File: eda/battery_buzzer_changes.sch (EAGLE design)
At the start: 15 parts, among them Q2 IRFML8244

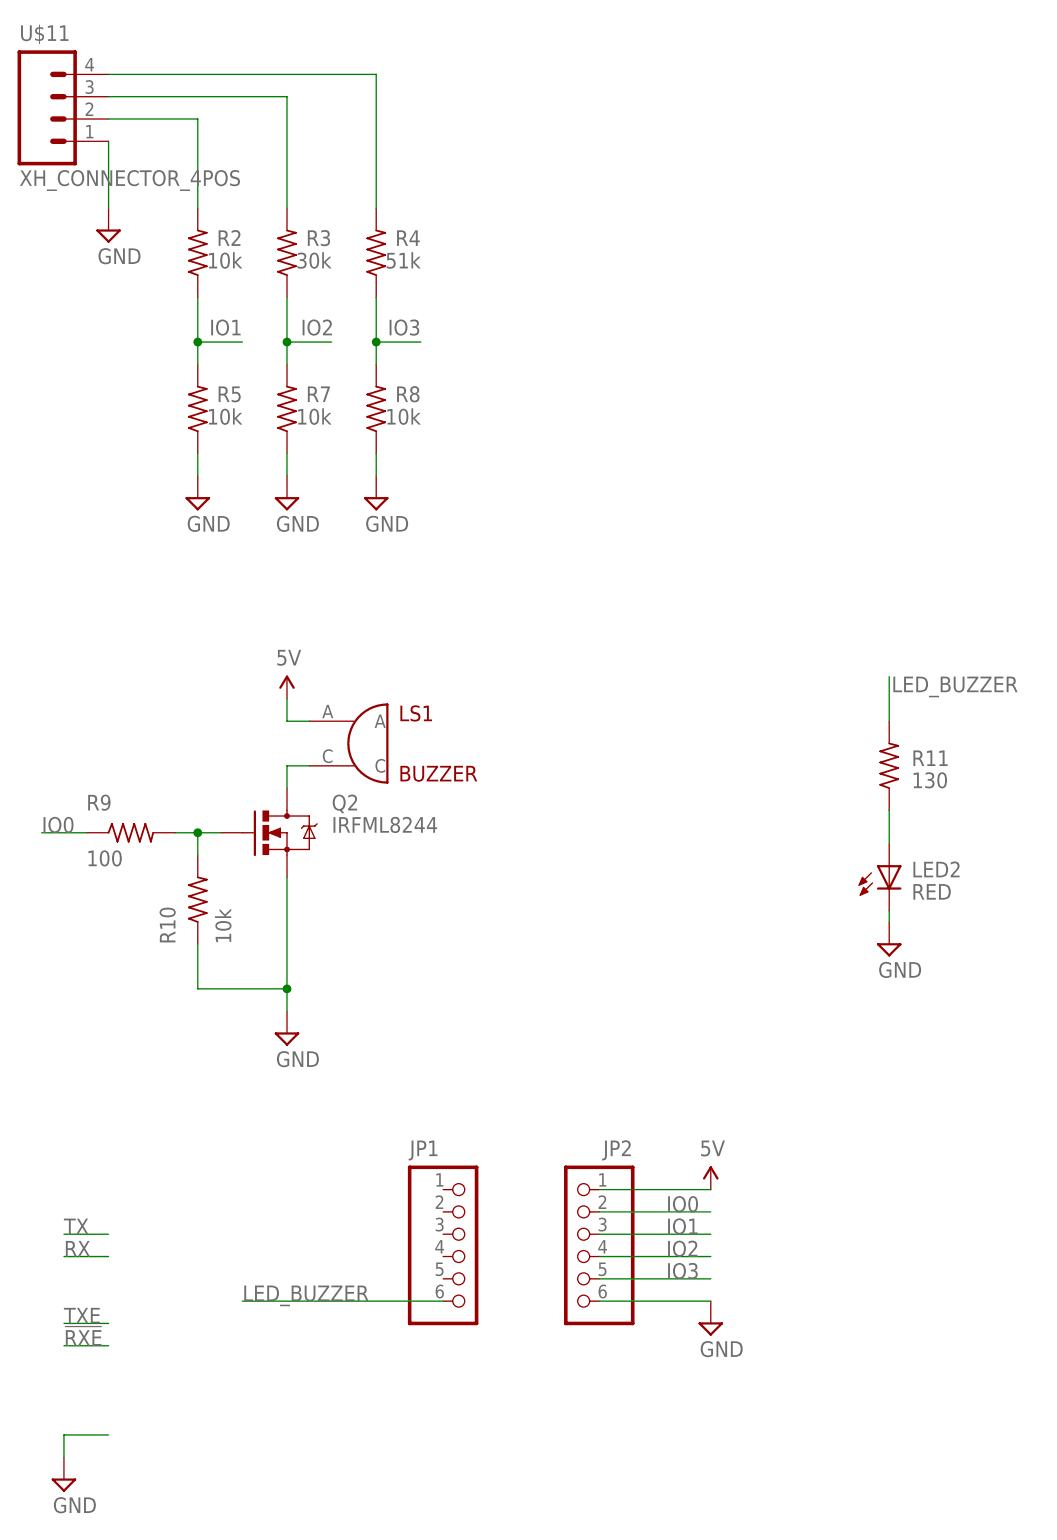
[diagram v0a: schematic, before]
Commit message: Battery Buzzer Changes
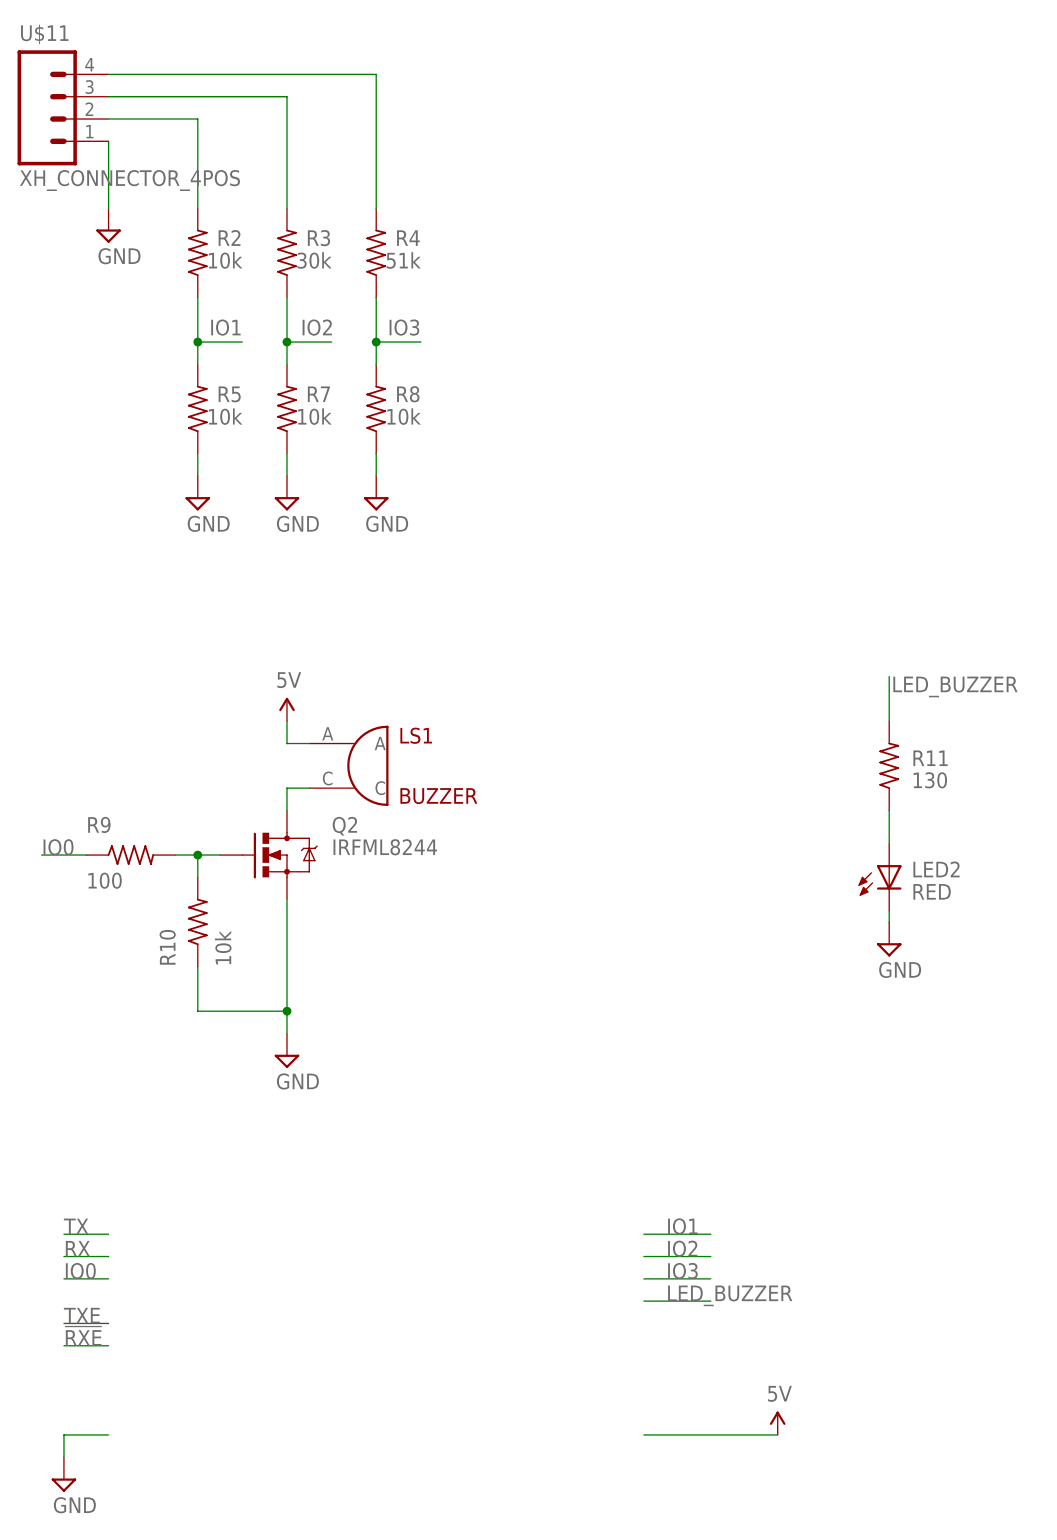
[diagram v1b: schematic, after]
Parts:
- removed JP1, JP2: (no value), pie:PINHD-1X6
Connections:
- net 5V: no longer JP2.1
- net IO0: no longer JP2.2
- net IO1: no longer JP2.3
- net IO2: no longer JP2.4
- net IO3: no longer JP2.5
- net LED_BUZZER: no longer JP1.6
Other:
- moved on the sheet: LS1, Q2, R10, R9
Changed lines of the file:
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@@
 <setting verticaltext="up"/>
 </settings>
-<grid distance="0.1" unitdist="inch" unit="inch" style="lines" multiple="1" display="yes" altdistance="0.01" altunitdist="inch" altunit="inch"/>
+<grid distance="0.1" unitdist="inch" unit="inch" style="lines" multiple="1" display="no" altdistance="0.01" altunitdist="inch" altunit="inch"/>
 <layers>
 <layer number="1" name="Top" color="4" fill="1" visible="no" active="no"/>
@@
 <part name="SUPPLY9" library="pie" deviceset="GND" device=""/>
 <part name="SUPPLY10" library="pie" deviceset="GND" device=""/>
+<part name="R11" library="pie" deviceset="R-US_" device="R0603" value="130"/>
+<part name="LED2" library="pie" deviceset="LED" device="0805" value="RED"/>
+<part name="SUPPLY13" library="pie" deviceset="GND" device=""/>
 <part name="LS1" library="pie" deviceset="BUZZER" device="" value="BUZZER"/>
 <part name="R9" library="pie" deviceset="R-US_" device="R0603" value="100"/>
@@
 <part name="U$12" library="pie" deviceset="5V" device=""/>
 <part name="SUPPLY11" library="pie" deviceset="GND" device=""/>
-<part name="R11" library="pie" deviceset="R-US_" device="R0603" value="130"/>
-<part name="LED2" library="pie" deviceset="LED" device="0805" value="RED"/>
-<part name="SUPPLY13" library="pie" deviceset="GND" device=""/>
 <part name="Q2" library="pie" deviceset="MOSFET-NCHANNEL" device="SMD" value="IRFML8244"/>
-<part name="JP1" library="pie" deviceset="PINHD-1X6" device=""/>
-<part name="JP2" library="pie" deviceset="PINHD-1X6" device=""/>
-<part name="SUPPLY2" library="pie" deviceset="GND" device=""/>
 </parts>
 <sheets>
@@
 </instance>
 <instance part="FRAME1" gate="G$2" x="147.32" y="0"/>
-<instance part="U$3" gate="G$1" x="88.9" y="43.18"/>
+<instance part="U$3" gate="G$1" x="96.52" y="15.24"/>
 <instance part="SUPPLY1" gate="GND" x="15.24" y="10.16"/>
 <instance part="U$11" gate="G$1" x="12.7" y="167.64"/>
@@
 <instance part="SUPPLY9" gate="GND" x="40.64" y="121.92"/>
 <instance part="SUPPLY10" gate="GND" x="50.8" y="121.92"/>
-<instance part="LS1" gate="G$1" x="48.26" y="93.98" smashed="yes">
-<attribute name="NAME" x="53.34" y="96.52" size="1.778" layer="94"/>
-<attribute name="VALUE" x="53.34" y="91.44" size="1.778" layer="94" align="top-left"/>
-</instance>
-<instance part="R9" gate="G$1" x="22.86" y="83.82"/>
-<instance part="R10" gate="G$1" x="30.48" y="76.2" rot="R90"/>
-<instance part="U$12" gate="G$1" x="40.64" y="99.06"/>
-<instance part="SUPPLY11" gate="GND" x="40.64" y="60.96"/>
 <instance part="R11" gate="G$1" x="109.22" y="91.44" smashed="yes" rot="R90">
 <attribute name="NAME" x="111.76" y="91.4146" size="1.778" layer="95" rot="MR0" align="bottom-right"/>
@@
 </instance>
 <instance part="SUPPLY13" gate="GND" x="109.22" y="71.12"/>
-<instance part="Q2" gate="G$1" x="40.64" y="83.82"/>
-<instance part="JP1" gate="A" x="58.42" y="36.83"/>
-<instance part="JP2" gate="A" x="76.2" y="36.83" rot="MR0"/>
-<instance part="SUPPLY2" gate="GND" x="88.9" y="27.94"/>
+<instance part="LS1" gate="G$1" x="48.26" y="91.44" smashed="yes">
+<attribute name="NAME" x="53.34" y="93.98" size="1.778" layer="94"/>
+<attribute name="VALUE" x="53.34" y="88.9" size="1.778" layer="94" align="top-left"/>
+</instance>
+<instance part="R9" gate="G$1" x="22.86" y="81.28"/>
+<instance part="R10" gate="G$1" x="30.48" y="73.66" rot="R90"/>
+<instance part="U$12" gate="G$1" x="40.64" y="96.52"/>
+<instance part="SUPPLY11" gate="GND" x="40.64" y="58.42"/>
+<instance part="Q2" gate="G$1" x="40.64" y="81.28"/>
 </instances>
 <busses>
@@
 <net name="5V" class="0">
 <segment>
+<pinref part="U$3" gate="G$1" pin="5V"/>
+<wire x1="81.28" y1="15.24" x2="96.52" y2="15.24" width="0.1524" layer="91"/>
+</segment>
+<segment>
 <pinref part="LS1" gate="G$1" pin="A"/>
 <pinref part="U$12" gate="G$1" pin="5V"/>
-<wire x1="43.18" y1="96.52" x2="40.64" y2="96.52" width="0.1524" layer="91"/>
-<wire x1="40.64" y1="96.52" x2="40.64" y2="99.06" width="0.1524" layer="91"/>
-</segment>
-<segment>
-<pinref part="U$3" gate="G$1" pin="5V"/>
-<pinref part="JP2" gate="A" pin="1"/>
-<wire x1="88.9" y1="43.18" x2="76.2" y2="43.18" width="0.1524" layer="91"/>
+<wire x1="43.18" y1="93.98" x2="40.64" y2="93.98" width="0.1524" layer="91"/>
+<wire x1="40.64" y1="93.98" x2="40.64" y2="96.52" width="0.1524" layer="91"/>
 </segment>
 </net>
@@
 </segment>
 <segment>
-<wire x1="40.64" y1="63.5" x2="40.64" y2="66.04" width="0.1524" layer="91"/>
-<pinref part="SUPPLY11" gate="GND" pin="GND"/>
-<wire x1="40.64" y1="66.04" x2="40.64" y2="78.74" width="0.1524" layer="91"/>
-<wire x1="30.48" y1="66.04" x2="40.64" y2="66.04" width="0.1524" layer="91"/>
-<junction x="40.64" y="66.04"/>
-<pinref part="Q2" gate="G$1" pin="S"/>
-<pinref part="R10" gate="G$1" pin="1"/>
-<wire x1="30.48" y1="71.12" x2="30.48" y2="66.04" width="0.1524" layer="91"/>
-</segment>
-<segment>
 <pinref part="LED2" gate="G$1" pin="C"/>
 <pinref part="SUPPLY13" gate="GND" pin="GND"/>
@@
 </segment>
 <segment>
-<wire x1="88.9" y1="30.48" x2="76.2" y2="30.48" width="0.1524" layer="91"/>
-<pinref part="SUPPLY2" gate="GND" pin="GND"/>
+<wire x1="40.64" y1="60.96" x2="40.64" y2="63.5" width="0.1524" layer="91"/>
+<pinref part="SUPPLY11" gate="GND" pin="GND"/>
+<wire x1="40.64" y1="63.5" x2="40.64" y2="76.2" width="0.1524" layer="91"/>
+<wire x1="30.48" y1="63.5" x2="40.64" y2="63.5" width="0.1524" layer="91"/>
+<junction x="40.64" y="63.5"/>
+<pinref part="Q2" gate="G$1" pin="S"/>
+<pinref part="R10" gate="G$1" pin="1"/>
+<wire x1="30.48" y1="68.58" x2="30.48" y2="63.5" width="0.1524" layer="91"/>
 </segment>
 </net>
@@
 <net name="IO1" class="0">
 <segment>
-<wire x1="76.2" y1="38.1" x2="88.9" y2="38.1" width="0.1524" layer="91"/>
+<wire x1="81.28" y1="38.1" x2="88.9" y2="38.1" width="0.1524" layer="91"/>
 <label x="83.82" y="38.1" size="1.778" layer="95"/>
-<pinref part="JP2" gate="A" pin="3"/>
 </segment>
 <segment>
@@
 <net name="IO2" class="0">
 <segment>
-<wire x1="76.2" y1="35.56" x2="88.9" y2="35.56" width="0.1524" layer="91"/>
+<wire x1="81.28" y1="35.56" x2="88.9" y2="35.56" width="0.1524" layer="91"/>
 <label x="83.82" y="35.56" size="1.778" layer="95"/>
-<pinref part="JP2" gate="A" pin="4"/>
 </segment>
 <segment>
@@
 <net name="IO0" class="0">
 <segment>
+<wire x1="20.32" y1="33.02" x2="15.24" y2="33.02" width="0.1524" layer="91"/>
+<label x="15.24" y="33.02" size="1.778" layer="95"/>
+</segment>
+<segment>
 <pinref part="R9" gate="G$1" pin="1"/>
-<wire x1="17.78" y1="83.82" x2="12.7" y2="83.82" width="0.1524" layer="91"/>
-<label x="12.7" y="83.82" size="1.778" layer="95"/>
-</segment>
-<segment>
-<label x="83.82" y="40.64" size="1.778" layer="95"/>
-<pinref part="JP2" gate="A" pin="2"/>
-<wire x1="76.2" y1="40.64" x2="88.9" y2="40.64" width="0.1524" layer="91"/>
+<wire x1="17.78" y1="81.28" x2="12.7" y2="81.28" width="0.1524" layer="91"/>
+<label x="12.7" y="81.28" size="1.778" layer="95"/>
 </segment>
 </net>
 <net name="IO3" class="0">
 <segment>
-<wire x1="76.2" y1="33.02" x2="88.9" y2="33.02" width="0.1524" layer="91"/>
+<wire x1="81.28" y1="33.02" x2="88.9" y2="33.02" width="0.1524" layer="91"/>
 <label x="83.82" y="33.02" size="1.778" layer="95"/>
-<pinref part="JP2" gate="A" pin="5"/>
 </segment>
 <segment>
@@
 </segment>
 </net>
-<net name="N$6" class="0">
-<segment>
-<pinref part="R9" gate="G$1" pin="2"/>
-<wire x1="33.02" y1="83.82" x2="30.48" y2="83.82" width="0.1524" layer="91"/>
-<pinref part="R10" gate="G$1" pin="2"/>
-<wire x1="30.48" y1="83.82" x2="27.94" y2="83.82" width="0.1524" layer="91"/>
-<wire x1="30.48" y1="81.28" x2="30.48" y2="83.82" width="0.1524" layer="91"/>
-<junction x="30.48" y="83.82"/>
-<pinref part="Q2" gate="G$1" pin="G"/>
-</segment>
-</net>
-<net name="N$5" class="0">
-<segment>
-<wire x1="40.64" y1="88.9" x2="40.64" y2="91.44" width="0.1524" layer="91"/>
-<pinref part="LS1" gate="G$1" pin="C"/>
-<wire x1="40.64" y1="91.44" x2="43.18" y2="91.44" width="0.1524" layer="91"/>
-<pinref part="Q2" gate="G$1" pin="D"/>
-</segment>
-</net>
 <net name="N$7" class="0">
 <segment>
@@
 </segment>
 <segment>
-<pinref part="JP1" gate="A" pin="6"/>
-<wire x1="58.42" y1="30.48" x2="35.56" y2="30.48" width="0.1524" layer="91"/>
-<label x="35.56" y="30.48" size="1.778" layer="95"/>
-</segment>
-</net>
+<wire x1="81.28" y1="30.48" x2="88.9" y2="30.48" width="0.1524" layer="91"/>
+<label x="83.82" y="30.48" size="1.778" layer="95"/>
+</segment>
+</net>
+<net name="N$6" class="0">
+<segment>
+<pinref part="R9" gate="G$1" pin="2"/>
+<wire x1="33.02" y1="81.28" x2="30.48" y2="81.28" width="0.1524" layer="91"/>
+<pinref part="R10" gate="G$1" pin="2"/>
+<wire x1="30.48" y1="81.28" x2="27.94" y2="81.28" width="0.1524" layer="91"/>
+<wire x1="30.48" y1="78.74" x2="30.48" y2="81.28" width="0.1524" layer="91"/>
+<junction x="30.48" y="81.28"/>
+<pinref part="Q2" gate="G$1" pin="G"/>
+</segment>
+</net>
+<net name="N$5" class="0">
+<segment>
+<wire x1="40.64" y1="86.36" x2="40.64" y2="88.9" width="0.1524" layer="91"/>
+<pinref part="LS1" gate="G$1" pin="C"/>
+<wire x1="40.64" y1="88.9" x2="43.18" y2="88.9" width="0.1524" layer="91"/>
+<pinref part="Q2" gate="G$1" pin="D"/>
+</segment>
+</net>
